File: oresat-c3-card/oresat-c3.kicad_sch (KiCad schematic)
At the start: 0 parts

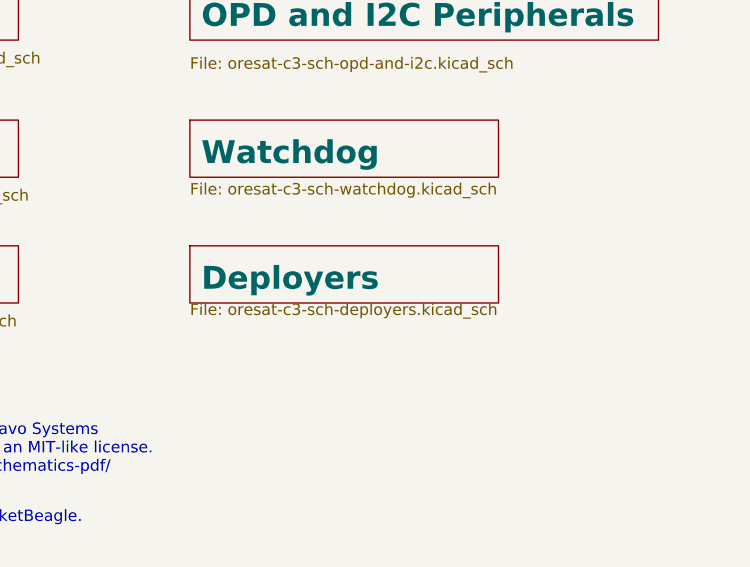
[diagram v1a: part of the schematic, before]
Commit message: started routing UHF and L band chip replacement on PCB
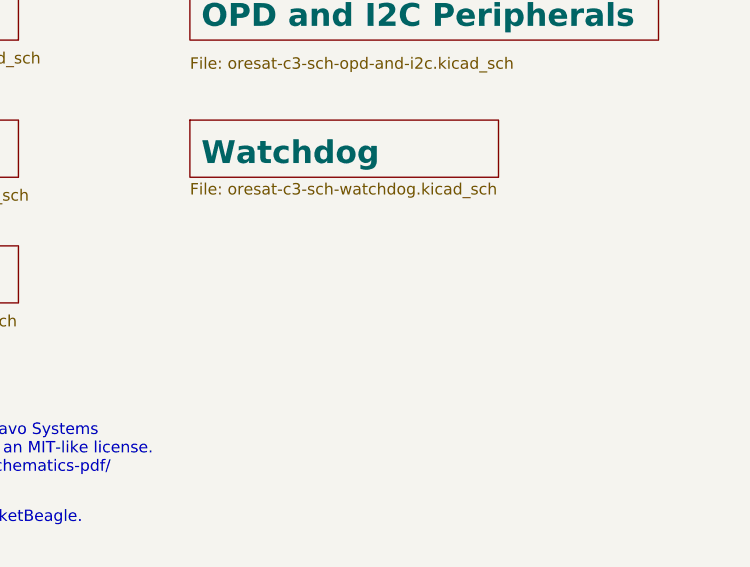
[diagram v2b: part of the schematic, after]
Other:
- removed sheet Deployers
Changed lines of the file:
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@@
-		)
-	)
-	(sheet
-		(at 247.65 153.67)
-		(size 34.29 6.35)
-		(exclude_from_sim no)
-		(in_bom yes)
-		(on_board yes)
-		(dnp no)
-		(stroke
-			(width 0.1524)
-			(type solid)
-		)
-		(fill
-			(color 0 0 0 0.0000)
-		)
-		(property "Sheetname" "Deployers"
-			(at 248.92 158.75 0)
-			(effects
-				(font
-					(size 2.54 2.54)
-					(bold yes)
-				)
-				(justify left bottom)
-			)
-		)
-		(property "Sheetfile" "oresat-c3-sch-deployers.kicad_sch"
-			(at 247.65 160.02 0)
-			(effects
-				(font
-					(size 1.27 1.27)
-				)
-				(justify left top)
-			)
-		)
-		(instances
-			(project "oresat-c3"
-				(path "/65d12cdd-c326-4033-9053-c59fa4e0b25e"
-					(page "12")
-				)
-			)
 		)
 	)
